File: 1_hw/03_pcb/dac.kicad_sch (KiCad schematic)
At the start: 2 parts

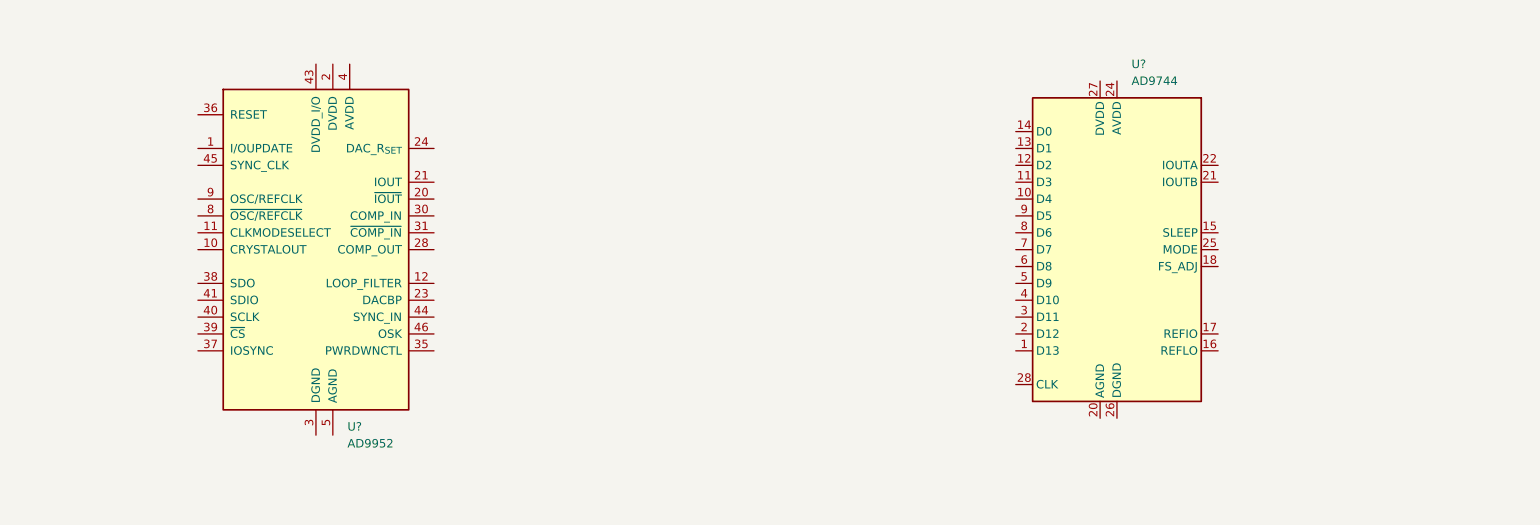
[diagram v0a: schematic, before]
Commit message: FEAT: Finished Excel Pin Map for MCU. Completed MCU + FPGA in Schematic.
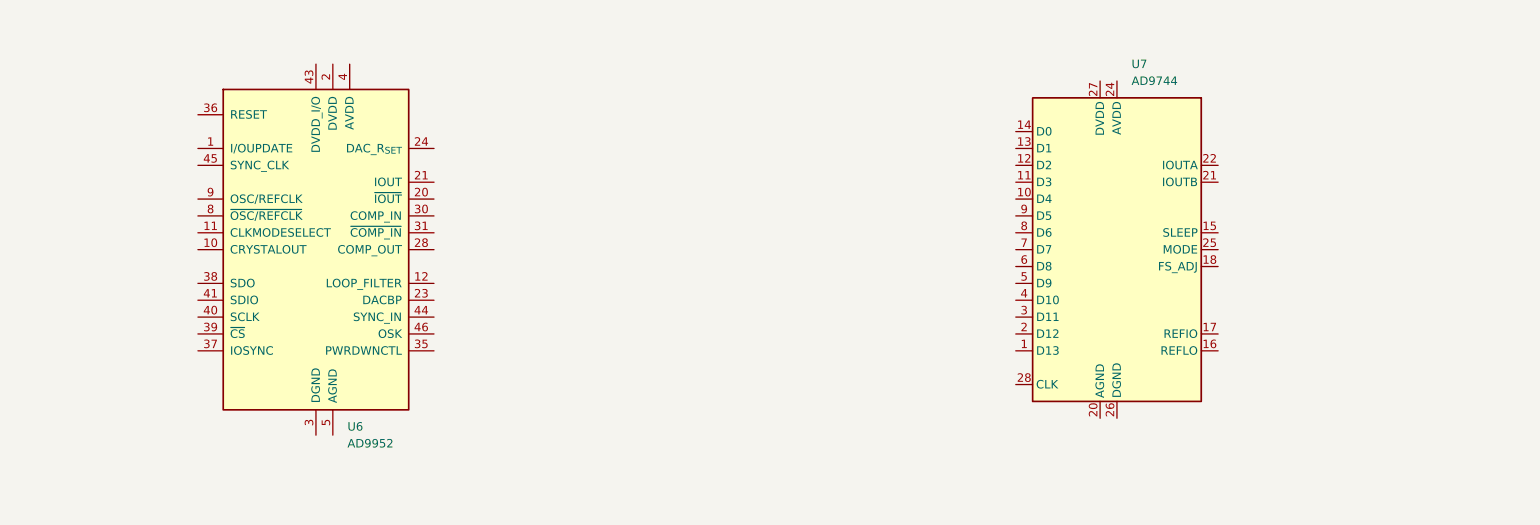
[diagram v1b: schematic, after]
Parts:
- gave numbers to parts that had none: 2
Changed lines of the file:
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@@
 		(dnp no)
 		(fields_autoplaced yes)
-		(property "Reference" "U?"
+		(property "Reference" "U6"
 			(at 93.6341 113.03 0)
 			(effects
@@
 			(project ""
 				(path "/866ef9be-3b01-4288-a6e0-a2357aa17e50/7126ceca-2dec-4994-855f-f217c0acdc71"
-					(reference "U?")
+					(reference "U6")
 					(unit 1)
 				)
@@
 		(dnp no)
 		(fields_autoplaced yes)
-		(property "Reference" "U?"
+		(property "Reference" "U7"
 			(at 211.7441 58.42 0)
 			(effects
@@
 			(project ""
 				(path "/866ef9be-3b01-4288-a6e0-a2357aa17e50/7126ceca-2dec-4994-855f-f217c0acdc71"
-					(reference "U?")
+					(reference "U7")
 					(unit 1)
 				)

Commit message: MINOR: Updated Block Diagram with preliminary post DAC stage analog design.
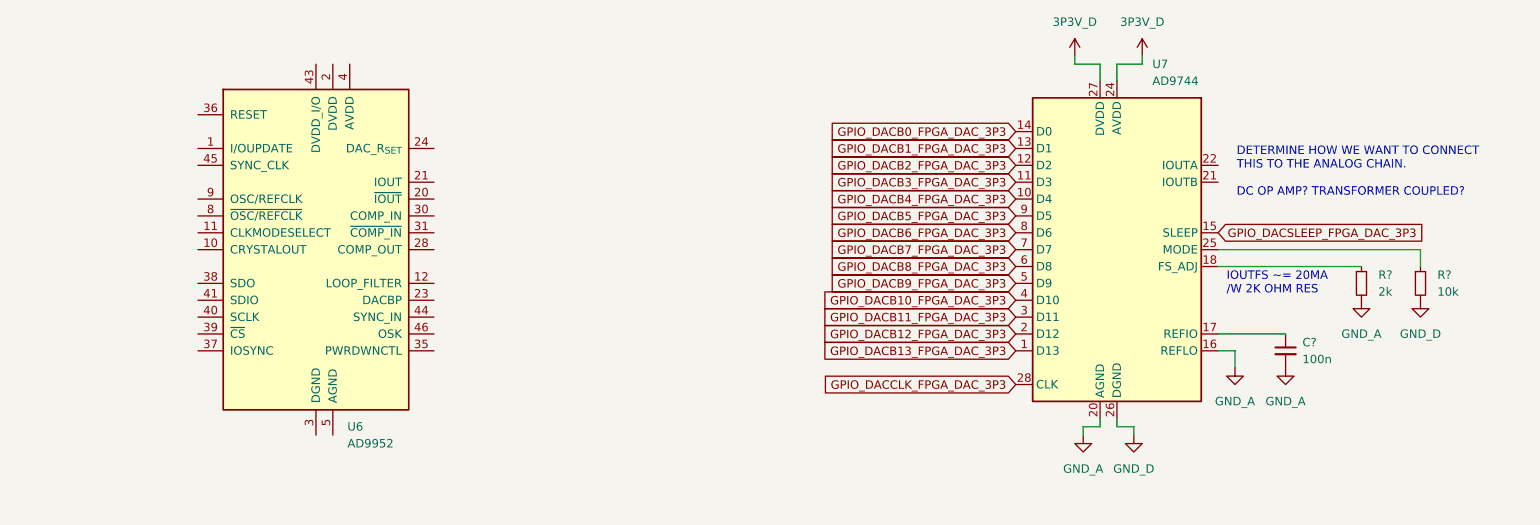
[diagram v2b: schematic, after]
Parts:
- added C?: 100n, Capacitor_SMD:C_0603_1608Metric, symbol Device:C_Small
- added R?: 10k, Resistor_SMD:R_0603_1608Metric, symbol Device:R_Small
- added R?: 2k, Resistor_SMD:R_0603_1608Metric, symbol Device:R_Small
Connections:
- net GPIO_DACB13_FPGA_DAC_3P3: now reaches U7.1 (D13)
- net GPIO_DACB4_FPGA_DAC_3P3: now reaches U7.10 (D4)
- net GPIO_DACB3_FPGA_DAC_3P3: now reaches U7.11 (D3)
- net GPIO_DACB2_FPGA_DAC_3P3: now reaches U7.12 (D2)
- net GPIO_DACB1_FPGA_DAC_3P3: now reaches U7.13 (D1)
- net GPIO_DACB0_FPGA_DAC_3P3: now reaches U7.14 (D0)
- net GPIO_DACSLEEP_FPGA_DAC_3P3: now reaches U7.15 (SLEEP)
- net GND_A: now reaches U7.16 (REFLO)
- net GND_A: now also U7.20 (AGND), C?.2, R?.2
- net at U7.17 (REFIO): now also C?.1
- net at U7.18 (FS_ADJ): now also R?.1
- net GPIO_DACB12_FPGA_DAC_3P3: now reaches U7.2 (D12)
- net 3P3V_D: now reaches U7.24 (AVDD)
- net 3P3V_D: now also U7.27 (DVDD)
- net at U7.25 (MODE): now also R?.1
- net GND_D: now reaches U7.26 (DGND)
- net GND_D: now also R?.2
- net GPIO_DACCLK_FPGA_DAC_3P3: now reaches U7.28 (CLK)
- net GPIO_DACB11_FPGA_DAC_3P3: now reaches U7.3 (D11)
- net GPIO_DACB10_FPGA_DAC_3P3: now reaches U7.4 (D10)
- net GPIO_DACB9_FPGA_DAC_3P3: now reaches U7.5 (D9)
- net GPIO_DACB8_FPGA_DAC_3P3: now reaches U7.6 (D8)
- net GPIO_DACB7_FPGA_DAC_3P3: now reaches U7.7 (D7)
- net GPIO_DACB6_FPGA_DAC_3P3: now reaches U7.8 (D6)
- net GPIO_DACB5_FPGA_DAC_3P3: now reaches U7.9 (D5)
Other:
- note added: "DETERMINE HOW WE WANT TO CONNECT THIS TO THE ANALOG CHAIN. DC OP AMP? TRANSFORMER COUPLED?"
- note added: "IOUTFS ~= 20MA /W 2K OHM RES"

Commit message: FEAT: Simulated Analog Paths, added first stage analog amp to schematic.
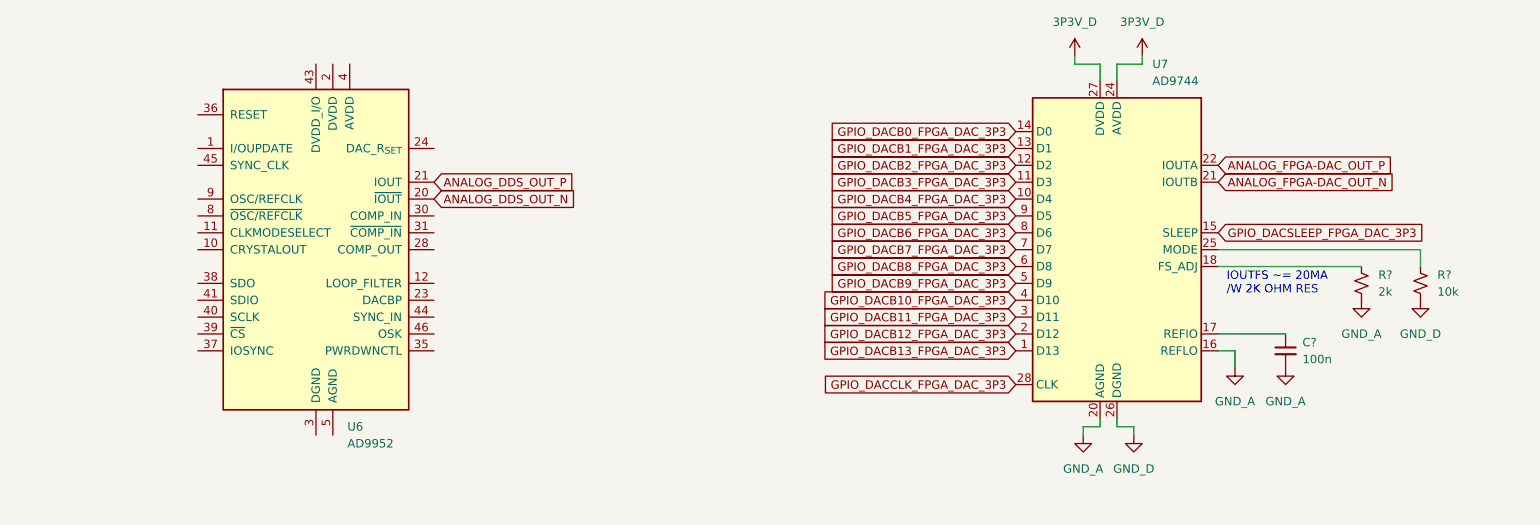
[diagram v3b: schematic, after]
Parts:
- R? (x2): symbol Device:R_Small -> Device:R_Small_US
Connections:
- net ANALOG_DDS_OUT_N: now reaches U6.20 (~{IOUT})
- net ANALOG_DDS_OUT_P: now reaches U6.21 (IOUT)
- net ANALOG_FPGA-DAC_OUT_N: now reaches U7.21 (IOUTB)
- net ANALOG_FPGA-DAC_OUT_P: now reaches U7.22 (IOUTA)
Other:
- note removed: "DETERMINE HOW WE WANT TO CONNECT THIS TO THE ANALOG CHAIN. DC OP AMP? TRANSFORMER COUPLED?"
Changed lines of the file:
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@@
 		(rev "0.0.1")
 		(company "Tomasz Brzyzek")
-		(comment 1 "Stasia Brzyzek")
 	)
 	(wire
@@
 		)
 	)
-	(text "DETERMINE HOW WE WANT TO CONNECT \nTHIS TO THE ANALOG CHAIN.\n\nDC OP AMP? TRANSFORMER COUPLED?"
-		(exclude_from_sim no)
-		(at 227.584 74.676 0)
+	(global_label "GPIO_DACB7_FPGA_DAC_3P3"
+		(shape input)
+		(at 194.31 86.36 180)
+		(fields_autoplaced yes)
+		(effects
+			(font
+				(size 1.27 1.27)
+			)
+			(justify right)
+		)
+		(property "Intersheetrefs" "${INTERSHEET_REFS}"
+			(at 164.8362 86.36 0)
+			(effects
+				(font
+					(size 1.27 1.27)
+				)
+				(justify right)
+				(hide yes)
+			)
+		)
+	)
+	(global_label "GPIO_DACSLEEP_FPGA_DAC_3P3"
+		(shape input)
+		(at 224.79 83.82 0)
+		(fields_autoplaced yes)
 		(effects
 			(font
@@
 			(justify left)
 		)
-	)
-	(global_label "GPIO_DACB7_FPGA_DAC_3P3"
-		(shape input)
-		(at 194.31 86.36 180)
-		(fields_autoplaced yes)
-		(effects
-			(font
-				(size 1.27 1.27)
-			)
-			(justify right)
-		)
-		(property "Intersheetrefs" "${INTERSHEET_REFS}"
-			(at 164.8362 86.36 0)
-			(effects
-				(font
-					(size 1.27 1.27)
-				)
-				(justify right)
-				(hide yes)
-			)
-		)
-	)
-	(global_label "GPIO_DACSLEEP_FPGA_DAC_3P3"
-		(shape input)
-		(at 224.79 83.82 0)
+		(property "Intersheetrefs" "${INTERSHEET_REFS}"
+			(at 257.5899 83.82 0)
+			(effects
+				(font
+					(size 1.27 1.27)
+				)
+				(justify left)
+				(hide yes)
+			)
+		)
+	)
+	(global_label "GPIO_DACB5_FPGA_DAC_3P3"
+		(shape input)
+		(at 194.31 81.28 180)
+		(fields_autoplaced yes)
+		(effects
+			(font
+				(size 1.27 1.27)
+			)
+			(justify right)
+		)
+		(property "Intersheetrefs" "${INTERSHEET_REFS}"
+			(at 164.8362 81.28 0)
+			(effects
+				(font
+					(size 1.27 1.27)
+				)
+				(justify right)
+				(hide yes)
+			)
+		)
+	)
+	(global_label "GPIO_DACB4_FPGA_DAC_3P3"
+		(shape input)
+		(at 194.31 78.74 180)
+		(fields_autoplaced yes)
+		(effects
+			(font
+				(size 1.27 1.27)
+			)
+			(justify right)
+		)
+		(property "Intersheetrefs" "${INTERSHEET_REFS}"
+			(at 164.8362 78.74 0)
+			(effects
+				(font
+					(size 1.27 1.27)
+				)
+				(justify right)
+				(hide yes)
+			)
+		)
+	)
+	(global_label "GPIO_DACB13_FPGA_DAC_3P3"
+		(shape input)
+		(at 194.31 101.6 180)
+		(fields_autoplaced yes)
+		(effects
+			(font
+				(size 1.27 1.27)
+			)
+			(justify right)
+		)
+		(property "Intersheetrefs" "${INTERSHEET_REFS}"
+			(at 163.6267 101.6 0)
+			(effects
+				(font
+					(size 1.27 1.27)
+				)
+				(justify right)
+				(hide yes)
+			)
+		)
+	)
+	(global_label "ANALOG_FPGA-DAC_OUT_N"
+		(shape input)
+		(at 224.79 76.2 0)
 		(fields_autoplaced yes)
 		(effects
@@
 		)
 		(property "Intersheetrefs" "${INTERSHEET_REFS}"
-			(at 257.5899 83.82 0)
+			(at 252.6916 76.2 0)
 			(effects
 				(font
@@
 		)
 	)
-	(global_label "GPIO_DACB5_FPGA_DAC_3P3"
-		(shape input)
-		(at 194.31 81.28 180)
-		(fields_autoplaced yes)
-		(effects
-			(font
-				(size 1.27 1.27)
-			)
-			(justify right)
-		)
-		(property "Intersheetrefs" "${INTERSHEET_REFS}"
-			(at 164.8362 81.28 0)
-			(effects
-				(font
-					(size 1.27 1.27)
-				)
-				(justify right)
-				(hide yes)
-			)
-		)
-	)
-	(global_label "GPIO_DACB4_FPGA_DAC_3P3"
-		(shape input)
-		(at 194.31 78.74 180)
-		(fields_autoplaced yes)
-		(effects
-			(font
-				(size 1.27 1.27)
-			)
-			(justify right)
-		)
-		(property "Intersheetrefs" "${INTERSHEET_REFS}"
-			(at 164.8362 78.74 0)
-			(effects
-				(font
-					(size 1.27 1.27)
-				)
-				(justify right)
-				(hide yes)
-			)
-		)
-	)
-	(global_label "GPIO_DACB13_FPGA_DAC_3P3"
-		(shape input)
-		(at 194.31 101.6 180)
-		(fields_autoplaced yes)
-		(effects
-			(font
-				(size 1.27 1.27)
-			)
-			(justify right)
-		)
-		(property "Intersheetrefs" "${INTERSHEET_REFS}"
-			(at 163.6267 101.6 0)
-			(effects
-				(font
-					(size 1.27 1.27)
-				)
-				(justify right)
-				(hide yes)
-			)
-		)
-	)
 	(global_label "GPIO_DACB11_FPGA_DAC_3P3"
 		(shape input)
@@
 		)
 	)
+	(global_label "ANALOG_DDS_OUT_N"
+		(shape input)
+		(at 106.68 78.74 0)
+		(fields_autoplaced yes)
+		(effects
+			(font
+				(size 1.27 1.27)
+			)
+			(justify left)
+		)
+		(property "Intersheetrefs" "${INTERSHEET_REFS}"
+			(at 128.4129 78.74 0)
+			(effects
+				(font
+					(size 1.27 1.27)
+				)
+				(justify left)
+				(hide yes)
+			)
+		)
+	)
 	(global_label "GPIO_DACB10_FPGA_DAC_3P3"
 		(shape input)
@@
 		)
 	)
+	(global_label "ANALOG_FPGA-DAC_OUT_P"
+		(shape input)
+		(at 224.79 73.66 0)
+		(fields_autoplaced yes)
+		(effects
+			(font
+				(size 1.27 1.27)
+			)
+			(justify left)
+		)
+		(property "Intersheetrefs" "${INTERSHEET_REFS}"
+			(at 252.6311 73.66 0)
+			(effects
+				(font
+					(size 1.27 1.27)
+				)
+				(justify left)
+				(hide yes)
+			)
+		)
+	)
 	(global_label "GPIO_DACCLK_FPGA_DAC_3P3"
 		(shape input)
@@
 				)
 				(justify right)
+				(hide yes)
+			)
+		)
+	)
+	(global_label "ANALOG_DDS_OUT_P"
+		(shape input)
+		(at 106.68 76.2 0)
+		(fields_autoplaced yes)
+		(effects
+			(font
+				(size 1.27 1.27)
+			)
+			(justify left)
+		)
+		(property "Intersheetrefs" "${INTERSHEET_REFS}"
+			(at 128.3524 76.2 0)
+			(effects
+				(font
+					(size 1.27 1.27)
+				)
+				(justify left)
 				(hide yes)
 			)
@@
 	)
 	(symbol
-		(lib_id "Device:R_Small")
+		(lib_id "Device:R_Small_US")
 		(at 255.27 91.44 0)
 		(unit 1)
@@
 		(fields_autoplaced yes)
 		(property "Reference" "R?"
-			(at 257.81 90.17 0)
+			(at 257.81 90.1699 0)
 			(effects
 				(font
@@
 		)
 		(property "Value" "10k"
-			(at 257.81 92.71 0)
+			(at 257.81 92.7099 0)
 			(effects
 				(font
@@
 			)
 		)
-		(property "Description" ""
+		(property "Description" "Resistor, small US symbol"
 			(at 255.27 91.44 0)
 			(effects
@@
 	)
 	(symbol
-		(lib_id "Device:R_Small")
+		(lib_id "Device:R_Small_US")
 		(at 246.38 91.44 0)
 		(unit 1)
@@
 		(fields_autoplaced yes)
 		(property "Reference" "R?"
-			(at 248.92 90.17 0)
+			(at 248.92 90.1699 0)
 			(effects
 				(font
@@
 		)
 		(property "Value" "2k"
-			(at 248.92 92.71 0)
+			(at 248.92 92.7099 0)
 			(effects
 				(font
@@
 			)
 		)
-		(property "Description" ""
+		(property "Description" "Resistor, small US symbol"
 			(at 246.38 91.44 0)
 			(effects

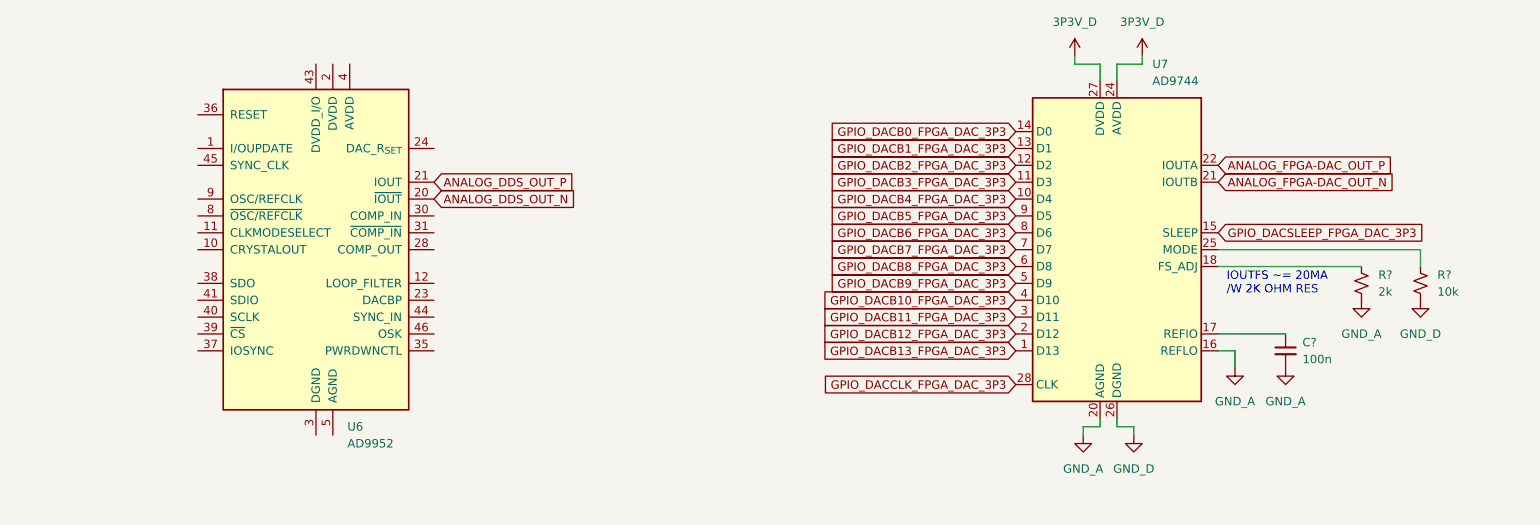
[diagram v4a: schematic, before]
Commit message: FEAT: Swapped out DDS IC and connected. Started adding Clockign Components into Schematic.
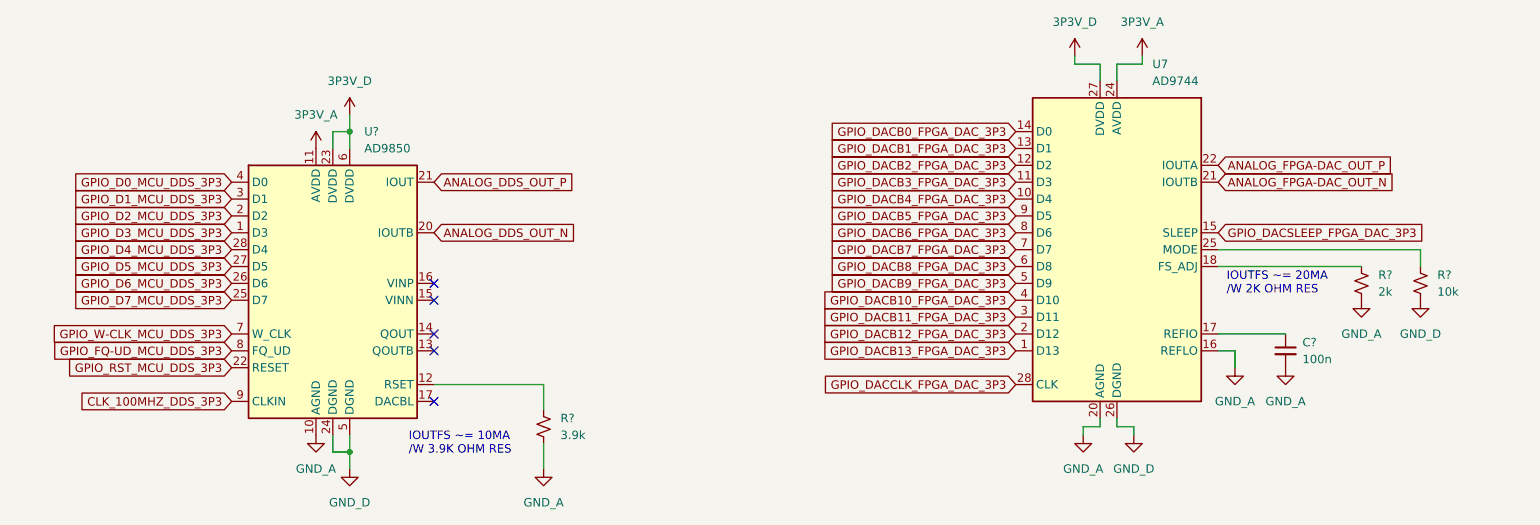
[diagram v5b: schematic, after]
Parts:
- removed U6: AD9952, Package_QFP:TQFP-48-1EP_7x7mm_P0.5mm_EP3.5x3.5mm, symbol BRZK_DAC:AD9952
- added R?: 3.9k, Resistor_SMD:R_0603_1608Metric, symbol Device:R_Small_US
- added U?: AD9850, Package_SO:SSOP-28_5.3x10.2mm_P0.65mm, symbol Interface:AD9850
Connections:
- net 3P3V_D: now also U?.23 (DVDD), U?.6 (DVDD); no longer U7.24 (AVDD)
- net ANALOG_DDS_OUT_N: now also U?.20 (IOUTB)
- net ANALOG_DDS_OUT_P: now also U?.21 (IOUT)
- net GND_A: now also R?.2, U?.10 (AGND), U?.19 (AGND)
- net GND_D: now also U?.24 (DGND), U?.5 (DGND)
- new net: R?.1, U?.12 (RSET)
- new net 3P3V_A: U7.24 (AVDD), U?.11 (AVDD), U?.18 (AVDD)
- new net CLK_100MHZ_DDS_3P3: U?.9 (CLKIN)
- new net GPIO_D0_MCU_DDS_3P3: U?.4 (D0)
- new net GPIO_D1_MCU_DDS_3P3: U?.3 (D1)
- new net GPIO_D2_MCU_DDS_3P3: U?.2 (D2)
- new net GPIO_D3_MCU_DDS_3P3: U?.1 (D3)
- new net GPIO_D4_MCU_DDS_3P3: U?.28 (D4)
- new net GPIO_D5_MCU_DDS_3P3: U?.27 (D5)
- new net GPIO_D6_MCU_DDS_3P3: U?.26 (D6)
- new net GPIO_D7_MCU_DDS_3P3: U?.25 (D7)
- new net GPIO_FQ-UD_MCU_DDS_3P3: U?.8 (FQ_UD)
- new net GPIO_RST_MCU_DDS_3P3: U?.22 (RESET)
- new net GPIO_W-CLK_MCU_DDS_3P3: U?.7 (W_CLK)
- no-connect marks 0 -> 5
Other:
- note added: "IOUTFS ~= 10MA /W 3.9K OHM RES"

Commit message: FEAT: Created Power Consumption Matrix.
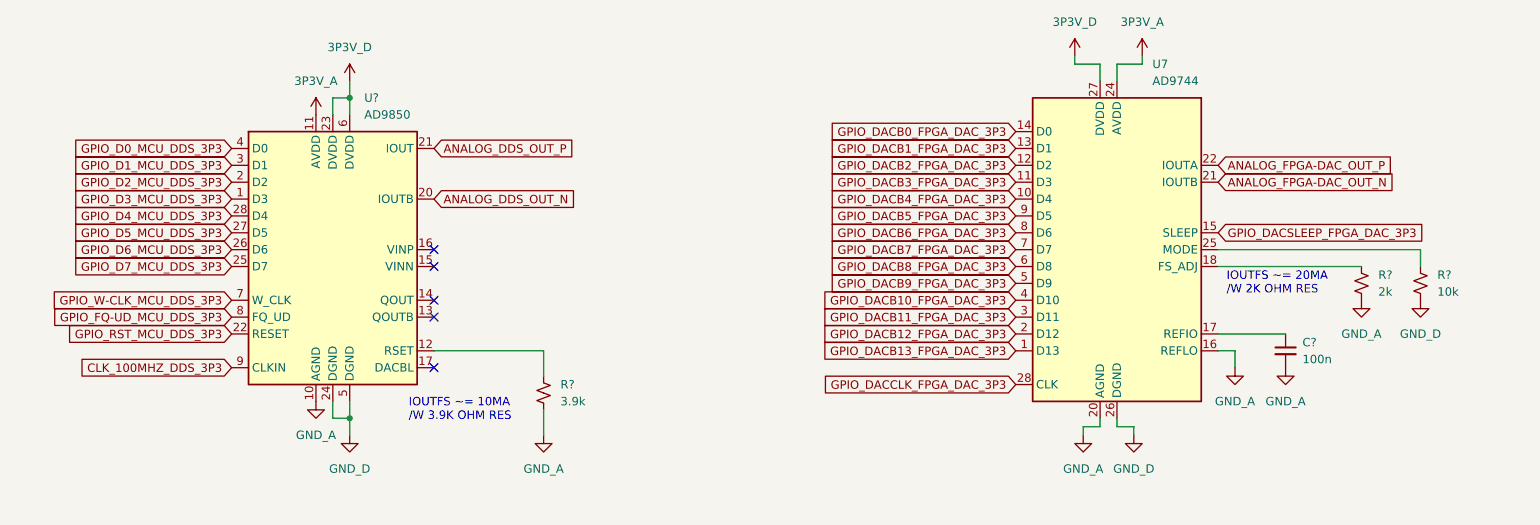
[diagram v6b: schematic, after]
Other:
- moved on the sheet: R?, U?
